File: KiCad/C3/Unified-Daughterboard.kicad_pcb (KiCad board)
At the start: 2 copper layers, 18 x 16.5 mm, 14 parts, among them J1 TYPE-C-31-M12_13, J2 SM04B-SRSS-TB(LF)(SN), U1 TPD4E05U06DQAR

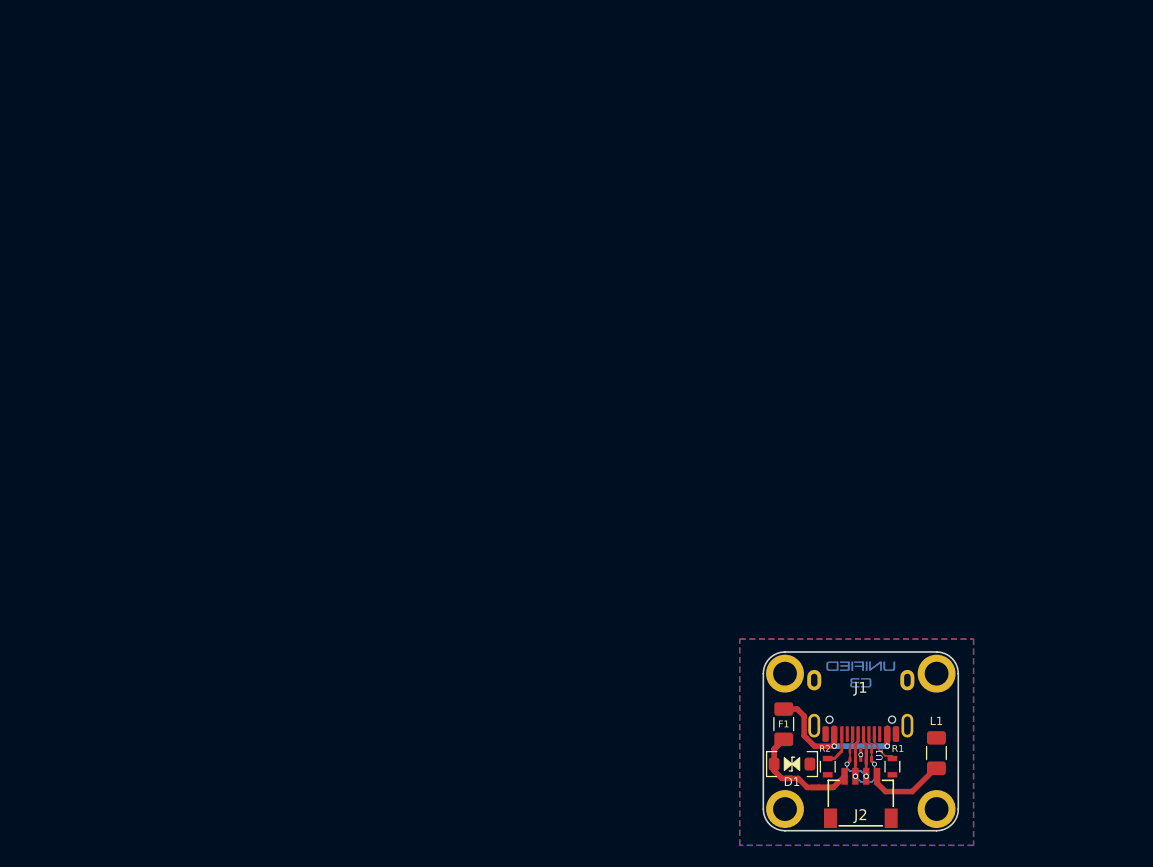
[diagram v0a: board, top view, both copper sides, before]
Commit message: 660 daughterboard outline and rearrangement
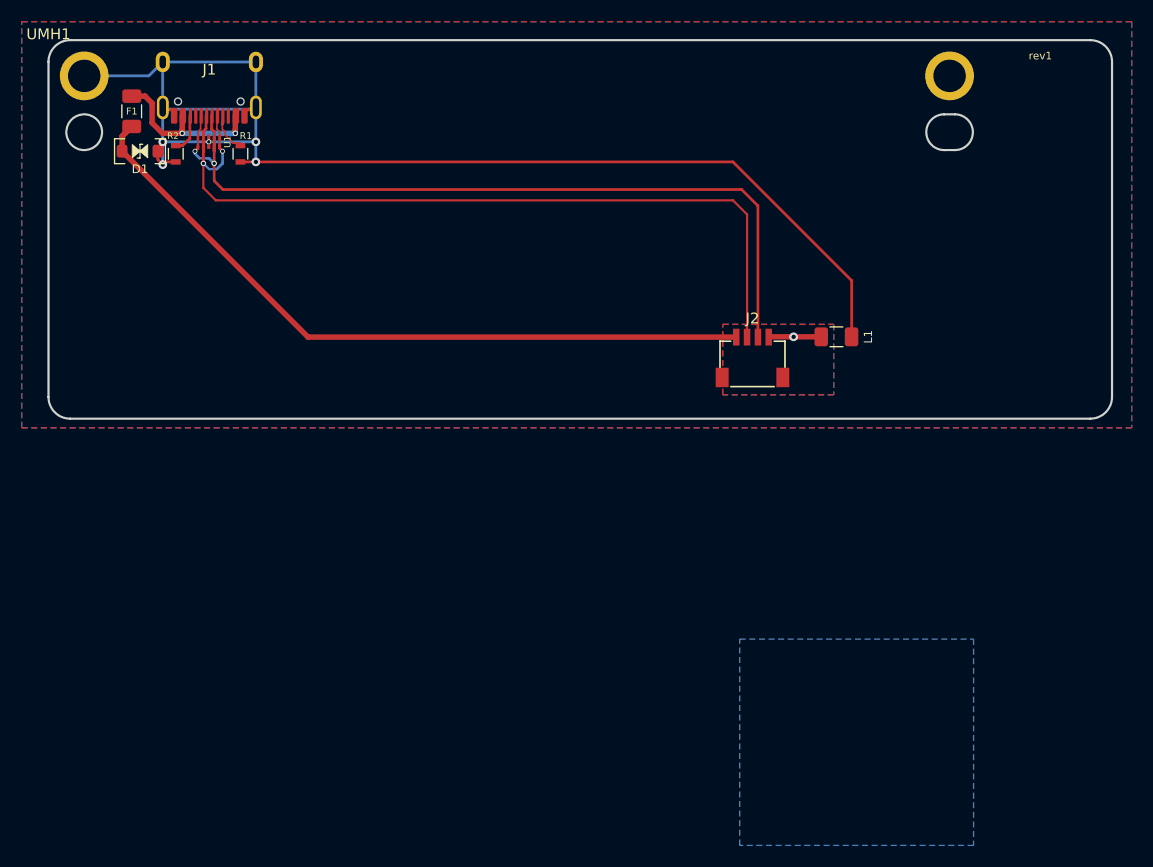
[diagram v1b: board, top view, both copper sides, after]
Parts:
- removed G1: Unified-Daughterboard-Logo, Unified-Daughterboard-Logo:Unified-Daughterboard-Logo.pretty
- removed G2: Unified-Daughterboard-Name, Unified-Daughterboard-Logo:Unified-Daughterboard-Name.pretty
- removed MH1, MH2, MH3, MH4: Mount-M2, random-keyboard-parts:Generic-Mounthole
- added NT1: NetTie_2, nopun-keyboard-parts:NetTie-2_SMD_Tiny, B.Cu at (15.2, 12.0)
- added NT2: NetTie_2, nopun-keyboard-parts:NetTie-2_SMD_Tiny, B.Cu at (14.3, 11.0)
- added UMH1: Outline, nopun-keyboard-parts:leopold_db_outline, F.Cu at (0.00, 0.00)
- J2: value SM04B-SRSS-TB(LF)(SN) -> JST Connector; footprint random-keyboard-parts:JST-SR-4 -> nopun-keyboard-parts:Jushuo-AFC10-SO4QCC-00-4x1-SMD-connector
- moved J1 82.9 mm to (14.9, 7.77)
- moved D1 82.6 mm to (8.45, 10.3)
- moved F1 82.6 mm to (7.69, 6.62)
- moved R1 82.6 mm to (17.7, 10.5)
- moved R2 82.6 mm to (11.8, 10.5)
- moved U1 82.6 mm to (14.8, 9.44)
- moved J2 41.8 mm to (65.0, 32.2)
- moved L1 39.5 mm to (72.8, 27.4), turned to 0 degrees
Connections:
- J1 pad A8: Net-(J1-PadA8) -> unconnected-(J1-PadA8)
- J1 pad B6: DA+ -> DB+
- J1 pad B7: DA- -> DB-
- J1 pad B8: Net-(J1-PadB8) -> unconnected-(J1-PadB8)
- U1 pad 1: DA+ -> DB+
- U1 pad 10: DA+ -> DB+
- U1 pad 5: DA- -> DB-
- U1 pad 6: DA- -> DB-
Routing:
- net GNDPWR: track 0.14 -> 123.6 mm, vias 1 -> 5
- net DA+: track 13.6 -> 73.3 mm, vias 2 -> 1
- net DA-: track 13.4 -> 71.9 mm, vias 2 -> 1
- net VCC: track 14.7 -> 67.5 mm
- net DB-: track 0.00 -> 5.41 mm, vias 0 -> 1
- net DB+: track 0.00 -> 4.36 mm, vias 0 -> 1
- net GND: track 7.36 -> 4.86 mm, vias 0 -> 1
- net Net-(J1-PadB5): track 6.33 -> 5.74 mm
- added copper zone on B.Cu, net GND
- added copper zone on F.Cu, net GND
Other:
- board size 18 x 16.5 mm -> 98.2 x 35 mm
- net class Default removed
- net class Power removed

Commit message: Trimmer version
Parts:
- UMH1: footprint nopun-keyboard-parts:leopold_db_outline -> nopun-keyboard-parts:leopold_db_trimmer
- moved L1 21.5 mm to (70.9, 6.06), turned to 90 degrees
- moved J2 20.0 mm to (65.0, 12.2)
- moved NT2 0.39 mm to (14.3, 11.3)
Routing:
- net DA+: track 73.3 -> 63.1 mm
- net DA-: track 71.9 -> 62.1 mm
- net GNDPWR: track 123.6 -> 116.2 mm
- net VCC: track 67.5 -> 66.1 mm
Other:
- board size 98.2 x 35 mm -> 88.5 x 15 mm
